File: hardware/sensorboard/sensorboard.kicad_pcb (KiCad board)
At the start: 2 copper layers, 46.9 x 19.2 mm, 17 parts, among them P1 PWR, P2 PROG, U1 ESP-07v2, U2 TC1262, U3 BMP180_board, U4 DHT22

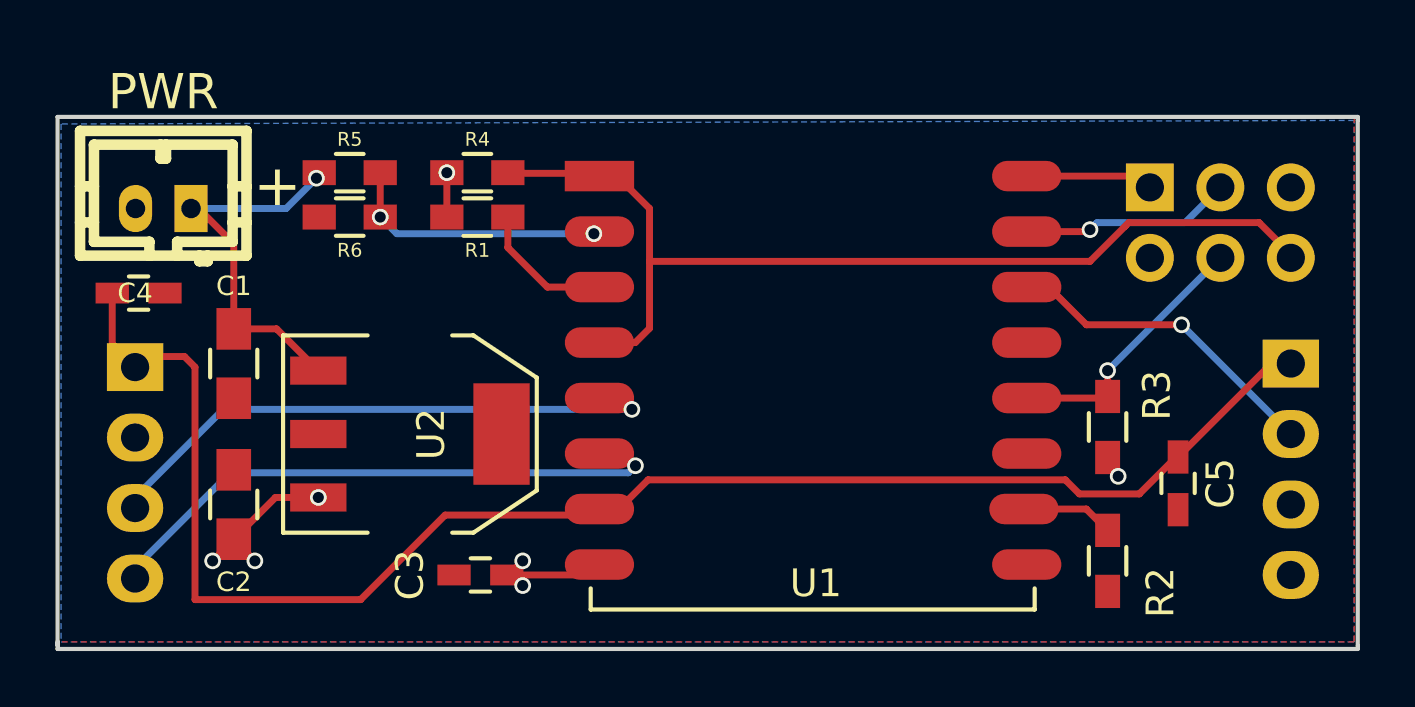
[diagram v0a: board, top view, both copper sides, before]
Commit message: Changed power connector, improved silkscreen.
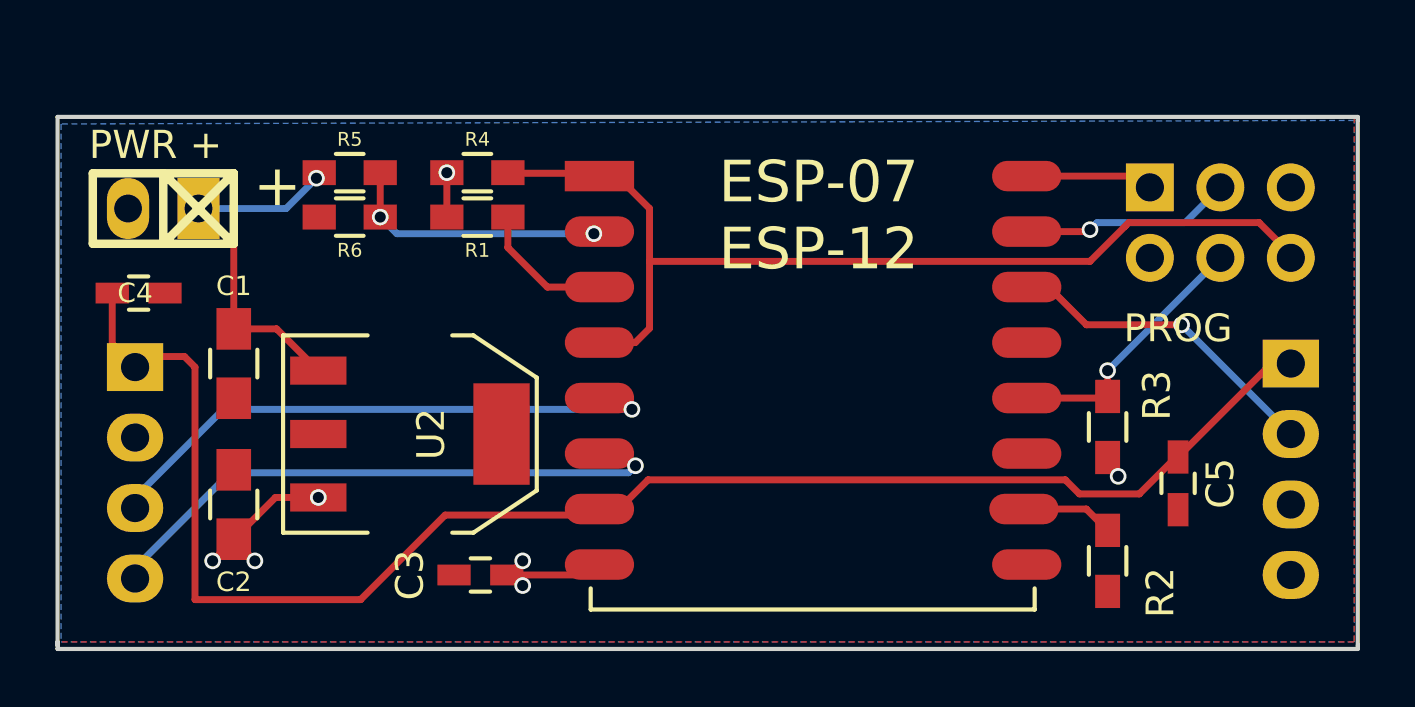
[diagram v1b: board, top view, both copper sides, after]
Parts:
- PWR +: renamed from P1; footprint w_conn_jst-ph:b2b-ph-kl -> w_pin_strip:pin_socket_2
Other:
- board text added: "DATA"
- board text added: "ESP-07 ESP-12"
- board text added: "GND"
- board text added: "PROG"
- board text added: "SCL"
- board text added: "SDA"
- board text added: "VIN"
- board text added: "bmp180"
- board text added: "◀ DHT22"
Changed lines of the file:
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@@
     (links 40)
     (no_connects 0)
-    (area 125.289 65.548599 175.208001 91.642001)
+    (area 128.194999 72.314999 175.208001 91.642001)
     (thickness 1.6)
-    (drawings 8)
+    (drawings 19)
     (tracks 110)
     (zones 0)
@@
     (descr "Through hole pin header")
     (tags "pin header")
-    (fp_text reference P2 (at 4.826 -2.794 540) (layer B.SilkS)
+    (fp_text reference P2 (at 4.826 -2.794 360) (layer B.SilkS) hide
       (effects (font (size 1 1) (thickness 0.15)) (justify mirror))
     )
@@
     (descr "Through hole pin header")
     (tags "pin header")
-    (fp_text reference U3 (at -0.09144 1.95326 360) (layer B.SilkS)
+    (fp_text reference U3 (at -0.09144 1.95326 180) (layer B.SilkS) hide
       (effects (font (size 1 1) (thickness 0.15)) (justify mirror))
     )
-    (fp_text value BMP180_board (at 0 3.1 180) (layer B.Fab)
+    (fp_text value BMP180_board (at 0 3.1 180) (layer B.SilkS) hide
       (effects (font (size 1 1) (thickness 0.15)) (justify mirror))
     )
@@
     (descr "Through hole pin header")
     (tags "pin header")
-    (fp_text reference U4 (at 2.413 -7.62 450) (layer B.SilkS)
+    (fp_text reference U4 (at 2.413 -7.62 270) (layer B.SilkS) hide
       (effects (font (size 1 1) (thickness 0.15)) (justify mirror))
     )
@@
     (descr "Module, ESP-8266, ESP-12, 16 pad, SMD")
     (tags "Module ESP-8266 ESP8266")
-    (fp_text reference U1 (at 7.0989 14.6764) (layer F.SilkS)
+    (fp_text reference U1 (at 7.0989 14.6764) (layer F.SilkS) hide
       (effects (font (size 1 1) (thickness 0.15)))
     )
@@
     )
   )
-  (module w_conn_jst-ph:b2b-ph-kl (layer F.Cu)
-    (at 132.08 75.692 180)
-    (descr "JST PH series connector, B2B-PH-KL")
-    (fp_text reference P1 (at 0 -2.99974 180) (layer F.SilkS) hide
-      (effects (font (thickness 0.3048)))
-    )
-    (fp_text value PWR (at 0 4.20116 180) (layer F.SilkS)
-      (effects (font (thickness 0.3048)))
-    )
-    (fp_line (start -0.09906 2.30124) (end -0.09906 1.80086) (layer F.SilkS) (width 0.381))
-    (fp_line (start -0.09906 1.80086) (end 0.09906 1.80086) (layer F.SilkS) (width 0.381))
-    (fp_line (start 0.09906 1.80086) (end 0.09906 2.30124) (layer F.SilkS) (width 0.381))
-    (fp_line (start 2.99974 -0.50038) (end 2.49936 -0.50038) (layer F.SilkS) (width 0.381))
-    (fp_line (start 2.49936 0.8001) (end 2.99974 0.8001) (layer F.SilkS) (width 0.381))
-    (fp_line (start -2.49936 0.8001) (end -2.99974 0.8001) (layer F.SilkS) (width 0.381))
-    (fp_line (start -2.49936 -0.50038) (end -2.99974 -0.50038) (layer F.SilkS) (width 0.381))
-    (fp_line (start -0.50038 -1.69926) (end -0.50038 -1.19888) (layer F.SilkS) (width 0.381))
-    (fp_line (start -0.50038 -1.19888) (end -2.49936 -1.19888) (layer F.SilkS) (width 0.381))
-    (fp_line (start -2.49936 -1.19888) (end -2.49936 2.30124) (layer F.SilkS) (width 0.381))
-    (fp_line (start -2.49936 2.30124) (end 2.49936 2.30124) (layer F.SilkS) (width 0.381))
-    (fp_line (start 2.49936 2.30124) (end 2.49936 -1.19888) (layer F.SilkS) (width 0.381))
-    (fp_line (start 2.49936 -1.19888) (end 0.50038 -1.19888) (layer F.SilkS) (width 0.381))
-    (fp_line (start 0.50038 -1.19888) (end 0.50038 -1.69926) (layer F.SilkS) (width 0.381))
-    (fp_line (start -2.99974 -1.69926) (end -2.99974 2.79908) (layer F.SilkS) (width 0.381))
-    (fp_line (start 2.99974 -1.69926) (end 2.99974 2.79908) (layer F.SilkS) (width 0.381))
-    (fp_line (start -1.30048 -1.69926) (end -1.30048 -1.89992) (layer F.SilkS) (width 0.381))
-    (fp_line (start -1.30048 -1.89992) (end -1.6002 -1.89992) (layer F.SilkS) (width 0.381))
-    (fp_line (start -1.6002 -1.89992) (end -1.6002 -1.69926) (layer F.SilkS) (width 0.381))
-    (fp_line (start 2.99974 -1.69926) (end -2.99974 -1.69926) (layer F.SilkS) (width 0.381))
-    (fp_line (start -2.99974 2.79908) (end 2.99974 2.79908) (layer F.SilkS) (width 0.381))
-    (pad 1 thru_hole rect (at -1.00076 0 180) (size 1.19888 1.69926) (drill 0.70104) (layers *.Cu *.Mask F.SilkS)
-      (net 1 +6V))
-    (pad 2 thru_hole oval (at 1.00076 0 180) (size 1.19888 1.69926) (drill 0.70104) (layers *.Cu *.Mask F.SilkS)
-      (net 2 GND))
-    (model walter/conn_jst-ph/b2b-ph-kl.wrl
-      (at (xyz 0 0 0))
-      (scale (xyz 1 1 1))
-      (rotate (xyz 0 0 0))
-    )
-  )
   (module Resistors_SMD:R_0603_HandSoldering (layer F.Cu)
     (at 138.8 74.4)
@@
     )
   )
+  (module w_pin_strip:pin_socket_2 (layer F.Cu)
+    (at 132.08 75.692 180)
+    (descr "Pin socket 2pin")
+    (tags "CONN DEV")
+    (fp_text reference "PWR +" (at 0.28 2.292 180) (layer F.SilkS)
+      (effects (font (size 1.016 1.016) (thickness 0.2032)))
+    )
+    (fp_text value PWR (at 0.254 -3.556 180) (layer F.SilkS) hide
+      (effects (font (size 1.016 0.889) (thickness 0.2032)))
+    )
+    (fp_line (start 0 -1.27) (end 0 1.27) (layer F.SilkS) (width 0.3048))
+    (fp_line (start 0 1.27) (end -2.54 -1.27) (layer F.SilkS) (width 0.3048))
+    (fp_line (start -2.54 1.27) (end 0 -1.27) (layer F.SilkS) (width 0.3048))
+    (fp_line (start 2.54 1.27) (end -2.54 1.27) (layer F.SilkS) (width 0.3048))
+    (fp_line (start -2.54 -1.27) (end 2.54 -1.27) (layer F.SilkS) (width 0.3048))
+    (fp_line (start -2.54 1.27) (end -2.54 -1.27) (layer F.SilkS) (width 0.3048))
+    (fp_line (start 2.54 -1.27) (end 2.54 1.27) (layer F.SilkS) (width 0.3048))
+    (pad 1 thru_hole rect (at -1.27 0 180) (size 1.524 2.19964) (drill 1.00076) (layers *.Cu *.Mask F.SilkS)
+      (net 1 +6V))
+    (pad 2 thru_hole oval (at 1.27 0 180) (size 1.524 2.19964) (drill 1.00076) (layers *.Cu *.Mask F.SilkS)
+      (net 2 GND))
+    (model walter/pin_strip/pin_socket_2.wrl
+      (at (xyz 0 0 0))
+      (scale (xyz 1 1 1))
+      (rotate (xyz 0 0 0))
+    )
+  )
+  (gr_text "ESP-07\nESP-12" (at 155.702 75.946) (layer F.SilkS)
+    (effects (font (size 1.5 1.5) (thickness 0.3)))
+  )
+  (gr_text PROG (at 168.656 80.01) (layer F.SilkS)
+    (effects (font (size 1 1) (thickness 0.25)))
+  )
+  (gr_text GND (at 168.656 88.9) (layer B.SilkS)
+    (effects (font (size 1.5 1.5) (thickness 0.3)) (justify mirror))
+  )
+  (gr_text DATA (at 168.402 83.82) (layer B.SilkS)
+    (effects (font (size 1.5 1.5) (thickness 0.3)) (justify mirror))
+  )
+  (gr_text VIN (at 169.164 81.28) (layer B.SilkS)
+    (effects (font (size 1.5 1.5) (thickness 0.3)) (justify mirror))
+  )
+  (gr_text "◀ DHT22\n" (at 166.116 86.614) (layer B.SilkS)
+    (effects (font (size 1.5 1.5) (thickness 0.3)) (justify mirror))
+  )
+  (gr_text SDA (at 135.382 89.154) (layer B.SilkS)
+    (effects (font (size 1.5 1.5) (thickness 0.3)) (justify mirror))
+  )
+  (gr_text SCL (at 135.382 86.614) (layer B.SilkS)
+    (effects (font (size 1.5 1.5) (thickness 0.3)) (justify mirror))
+  )
+  (gr_text "GND\n" (at 135.382 83.82) (layer B.SilkS)
+    (effects (font (size 1.5 1.5) (thickness 0.3)) (justify mirror))
+  )
+  (gr_text VIN (at 134.874 81.28) (layer B.SilkS)
+    (effects (font (size 1.5 1.5) (thickness 0.3)) (justify mirror))
+  )
+  (gr_text bmp180 (at 133.604 78.486) (layer B.SilkS)
+    (effects (font (size 1.5 1.5) (thickness 0.3)) (justify mirror))
+  )
   (gr_line (start 175.133 72.39) (end 175.133 72.517) (angle 90) (layer Edge.Cuts) (width 0.15))
   (gr_line (start 128.27 72.39) (end 175.133 72.39) (angle 90) (layer Edge.Cuts) (width 0.15))
@@
   (segment (start 134.62 80.03) (end 136.164 80.03) (width 0.25) (layer F.Cu) (net 1))
   (segment (start 136.164 80.03) (end 137.668 81.534) (width 0.25) (layer F.Cu) (net 1))
-  (segment (start 142.3 74.4) (end 142.3 76) (width 0.25) (layer F.Cu) (net 3) (status C00000))
-  (via (at 142.3 74.4) (size 0.6) (drill 0.4) (layers F.Cu B.Cu) (net 3) (status C00000))
+  (segment (start 142.3 74.4) (end 142.3 76) (width 0.25) (layer F.Cu) (net 3))
+  (via (at 142.3 74.4) (size 0.6) (drill 0.4) (layers F.Cu B.Cu) (net 3))
   (segment (start 142.41 74.422) (end 142.24 74.422) (width 0.25) (layer F.Cu) (net 3))
   (segment (start 144.46 88.9) (end 144.653 88.9) (width 0.25) (layer F.Cu) (net 3))
@@
   (segment (start 144.61 74.422) (end 148.3995 74.422) (width 0.25) (layer F.Cu) (net 8))
   (segment (start 148.3995 74.422) (end 148.5011 74.5236) (width 0.25) (layer F.Cu) (net 8))
-  (segment (start 144.5 76) (end 144.5 77.1) (width 0.25) (layer F.Cu) (net 9) (status 400000))
-  (segment (start 145.9236 78.5236) (end 148.5011 78.5236) (width 0.25) (layer F.Cu) (net 9) (status 800000))
+  (segment (start 144.5 76) (end 144.5 77.1) (width 0.25) (layer F.Cu) (net 9))
+  (segment (start 145.9236 78.5236) (end 148.5011 78.5236) (width 0.25) (layer F.Cu) (net 9))
   (segment (start 144.5 77.1) (end 145.9236 78.5236) (width 0.25) (layer F.Cu) (net 9))
   (segment (start 148.4635 78.486) (end 148.5011 78.5236) (width 0.25) (layer F.Cu) (net 9))

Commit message: Improved silkscreening for sensorboard.
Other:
- board text added: "ESP sensorboard v2.2"
- board text added: "z2amiller"
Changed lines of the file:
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@@
-(kicad_pcb (version 4) (host pcbnew "(2015-09-17 BZR 6202)-product")
+(kicad_pcb (version 4) (host pcbnew "(2015-10-28 BZR 6285)-product")
   (general
     (links 40)
     (no_connects 0)
-    (area 128.194999 72.314999 175.208001 91.642001)
+    (area 125.289 65.548599 175.208001 91.642001)
     (thickness 1.6)
-    (drawings 19)
+    (drawings 21)
     (tracks 110)
     (zones 0)
@@
       (drillshape 0)
       (scaleselection 1)
-      (outputdirectory /Users/amiller/projects/sensorboard/hardware/sensorboard/gerber/))
+      (outputdirectory /Users/armil/projects/sensorboard/hardware/sensorboard/gerber/))
   )
   (net 0 "")
@@
     )
   )
+  (gr_text "ESP sensorboard v2.2" (at 153.2 74) (layer B.SilkS)
+    (effects (font (size 1.5 1.5) (thickness 0.3)) (justify mirror))
+  )
+  (gr_text "z2amiller\n" (at 152.4 89.8) (layer B.SilkS)
+    (effects (font (size 1.5 1.5) (thickness 0.3)) (justify mirror))
+  )
   (gr_text "ESP-07\nESP-12" (at 155.702 75.946) (layer F.SilkS)
